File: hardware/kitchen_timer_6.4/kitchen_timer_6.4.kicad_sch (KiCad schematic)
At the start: 56 parts, among them J1 USB_C, J2 BREAKOUT, J3 JST PH 2.0, Q1 MMBT2222A, Q2 MMBT2222A, Q3 MMBT2222A, Q4 MMBT2222A, Q5 MMBT2222A, SW1 VOLUME, SW2 FUNCTION_SELECTOR, SW3 ON/OFF, SW4 SECONDS, SW5 MINUTES, SW6 RESET_TIME, SW7 START/STOP, U1 DIO5518B, U2 TPS613222ADBV, U3 ATmega4808-A, U4 LTC-5723HR

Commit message: extra capacitor
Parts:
- added C4: 10u, 00_local:C_0805_2012Metric_Pad1.18x1.45mm_HandSolder, symbol 00_local:C
- renumbered C4 to C1, C5 to C2, C1 to C3, C2 to C5, C3 to C6, D3 to D2, D2 to D3, J3 to J1, J1 to J2, J2 to J3, Q2 to Q1, Q3 to Q2, Q4 to Q3, Q5 to Q4, Q1 to Q5, R10 to R1, R4 to R10, R18 to R11, R1 to R12, R19 to R13, R7 to R14, R20 to R15, R9 to R16, R21 to R17, R5 to R18, R6 to R19, R11 to R2, R3 to R20, R8 to R21, R12 to R3, R13 to R4, R14 to R5, R15 to R6, R16 to R7, R17 to R8, R2 to R9, SW3 to SW1, SW4 to SW2, SW5 to SW3, SW6 to SW4, SW1 to SW5, SW7 to SW6, SW2 to SW7, U4 to U1, U3 to U2, U1 to U3, U2 to U4
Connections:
- net BAT+: now also C4.1
- net GND: now also C4.2
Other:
- moved on the sheet: C3

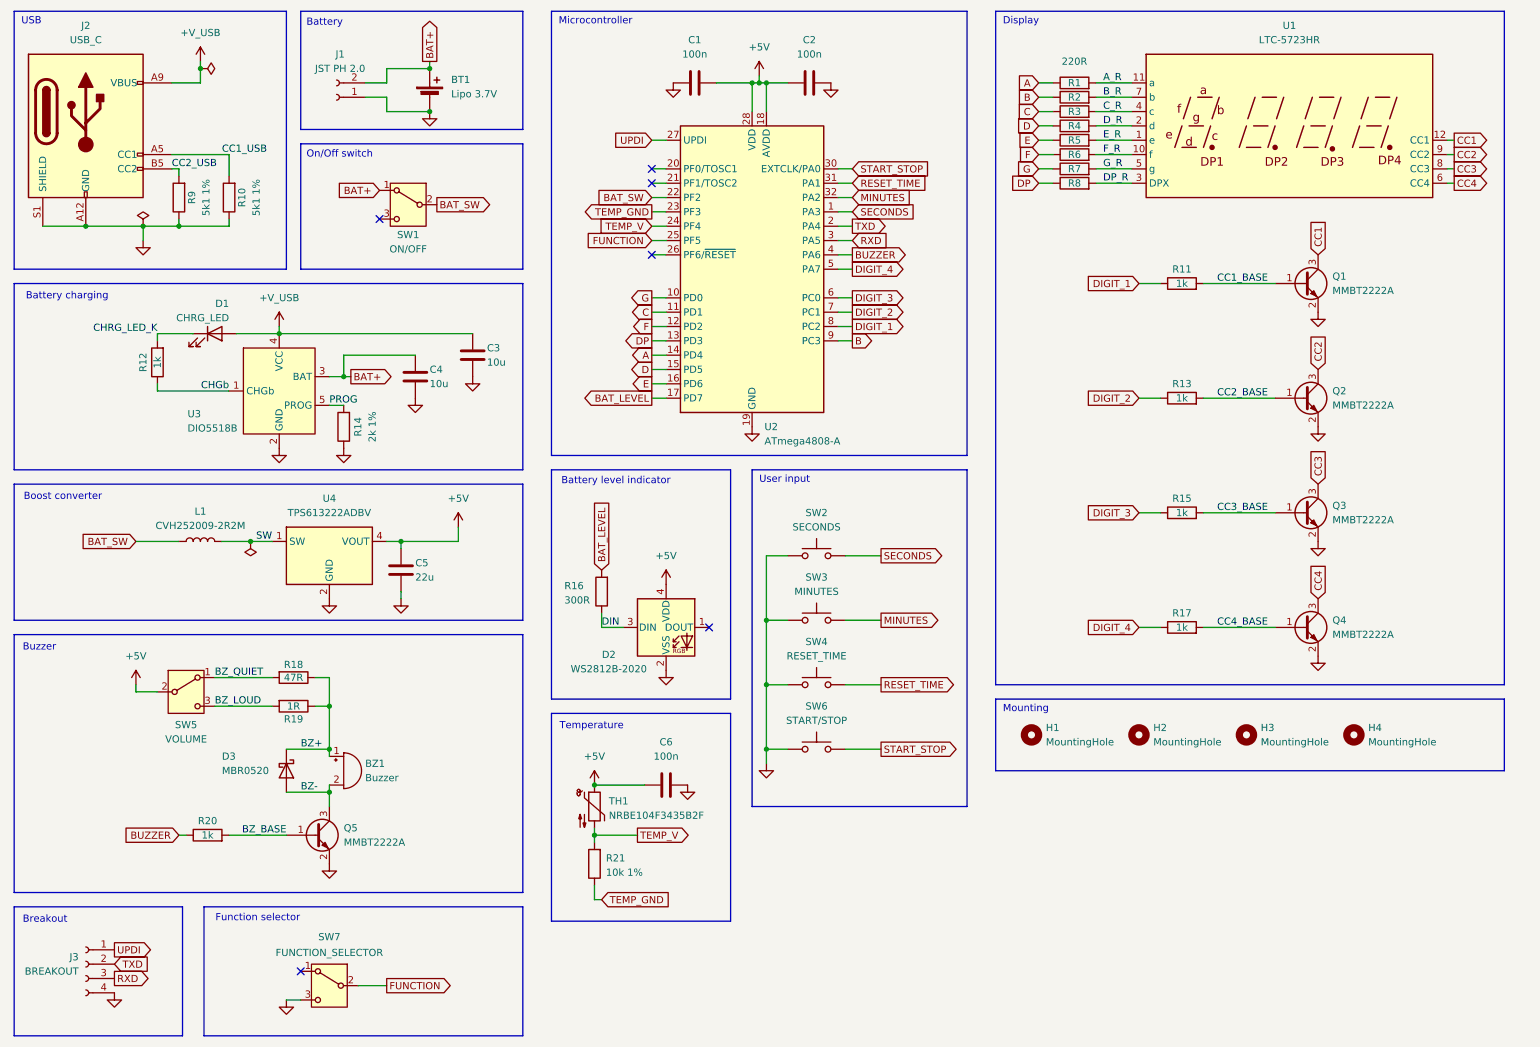
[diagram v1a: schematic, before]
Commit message: redid the schematic without reannotating.  Hoping to me the usb -> battery charger -> boost converter more clear
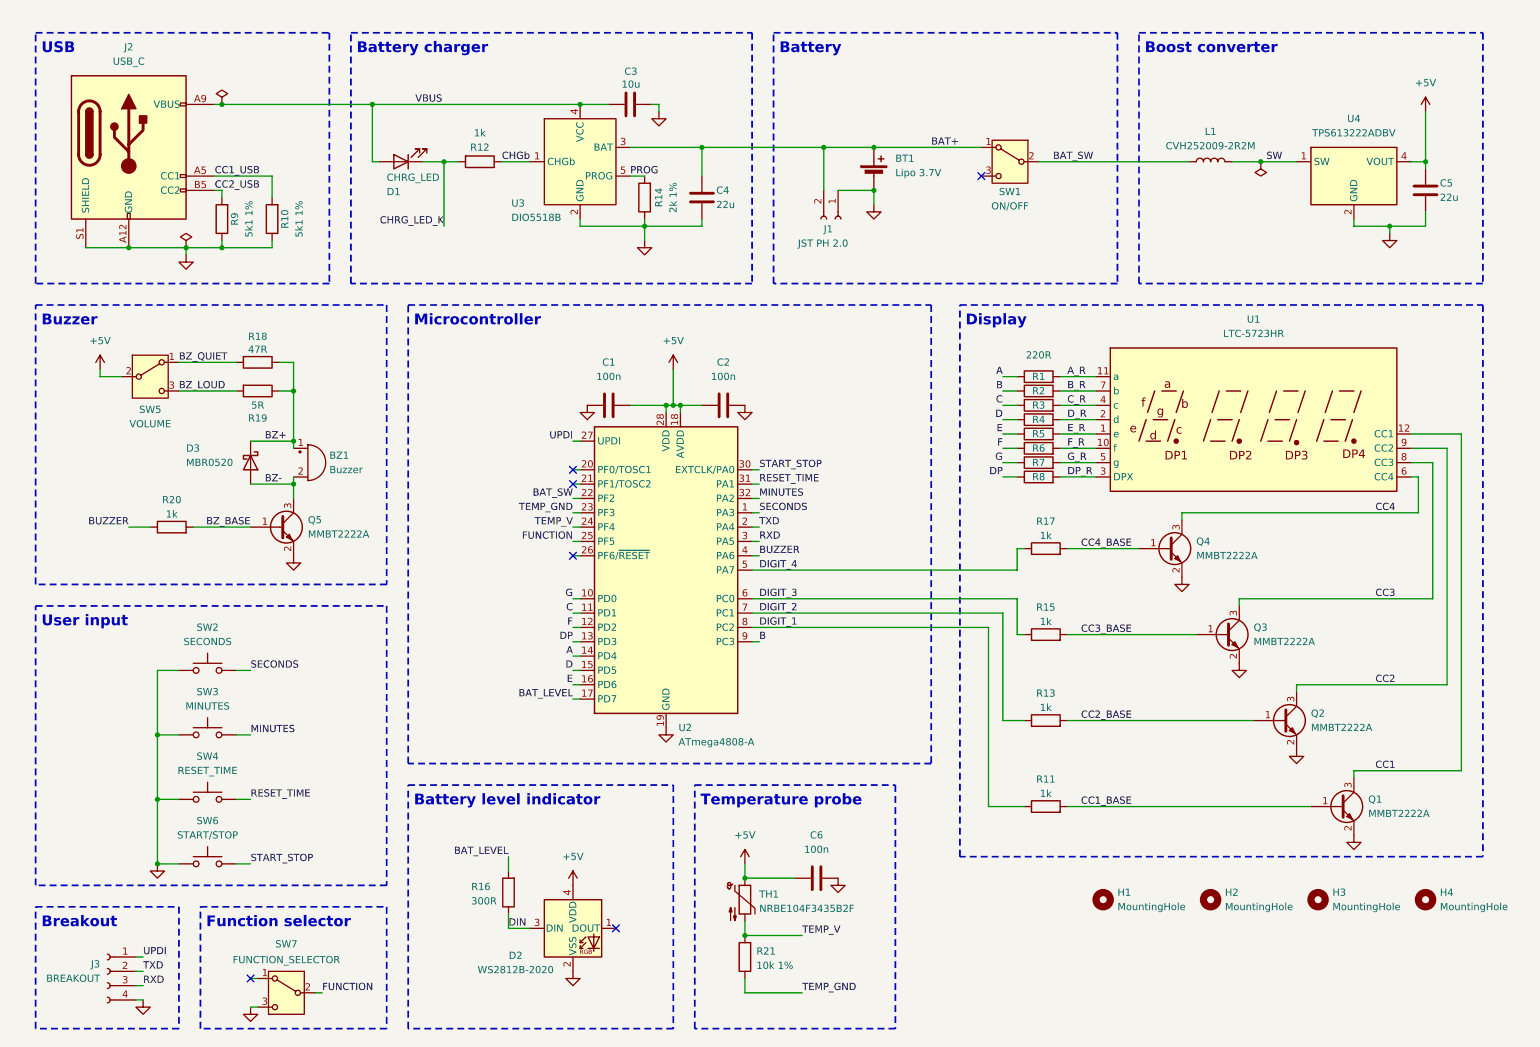
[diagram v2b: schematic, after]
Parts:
- C4: value 10u -> 22u
- R19: value 1R -> 5R
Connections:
- net +V_USB renamed VBUS
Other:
- note added: "Battery charger"
- note added: "Temperature probe"
- note removed: "Battery charging"
- note removed: "Mounting"
- note removed: "On/Off switch"
- note removed: "Temperature"
- moved on the sheet: BT1, BZ1, C1, C2, C3, C4, C5, C6, D1, D2, D3, H1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
